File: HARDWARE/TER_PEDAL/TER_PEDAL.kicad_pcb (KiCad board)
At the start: 4 copper layers, 78.2 x 40 mm, 63 parts, among them J1 DEBUG, J2 APPS_1, J3 RJ45_Shielded, J4 APPS_2, J5 BPPS_1, SW1 RST, U1 STM32F103C8Tx, U2 AOZ1280CI, U3 LM1117MP-3.3, U4 SN65HVD230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

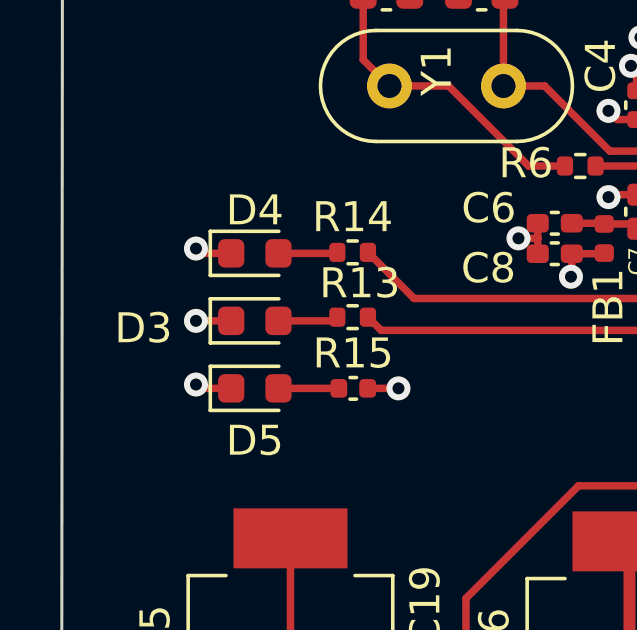
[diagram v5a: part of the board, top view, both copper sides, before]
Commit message: Changed Pinout and added status leds silkmask
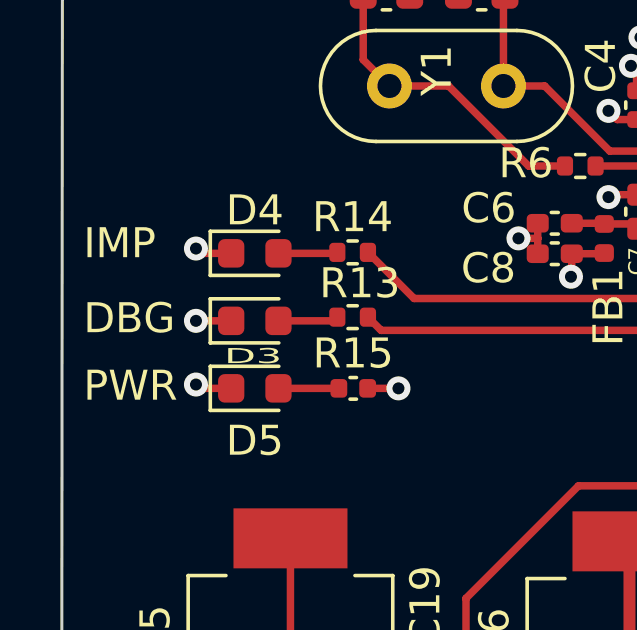
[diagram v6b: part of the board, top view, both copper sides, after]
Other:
- board text added: "DBG"
- board text added: "IMP"
- board text added: "PWR"
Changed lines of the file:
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@@
     (property "ki_keywords" "LED diode")
     (attr smd)
-    (fp_text reference "D3" (at -3.7125 0.25) (layer "F.SilkS")
-        (effects (font (size 1 1) (thickness 0.15)))
+    (fp_text reference "D3" (at -0.056699 1.175611) (layer "F.SilkS")
+        (effects (font (size 0.5 1) (thickness 0.125)))
     )
     (fp_text value "LED" (at 0 1.43) (layer "F.Fab")
@@
   (gr_line (start 114.3 75) (end 187.5 75)
     (stroke (width 0.1) (type default)) (layer "Edge.Cuts"))
+  (gr_text "PWR\n" (at 112.5 93.75) (layer "F.SilkS")
+    (effects (font (size 1 1) (thickness 0.15)) (justify left bottom))
+  )
+  (gr_text "IMP" (at 112.5 89) (layer "F.SilkS")
+    (effects (font (size 1 1) (thickness 0.15)) (justify left bottom))
+  )
+  (gr_text "DBG" (at 112.5 91.5) (layer "F.SilkS")
+    (effects (font (size 1 1) (thickness 0.15)) (justify left bottom))
+  )
   (segment (start 139.6715 91.3335) (end 139.43 91.092) (width 0.25) (layer "F.Cu") (net 1))
   (segment (start 140.8425 83.342) (end 141.93 83.342) (width 0.25) (layer "F.Cu") (net 1))

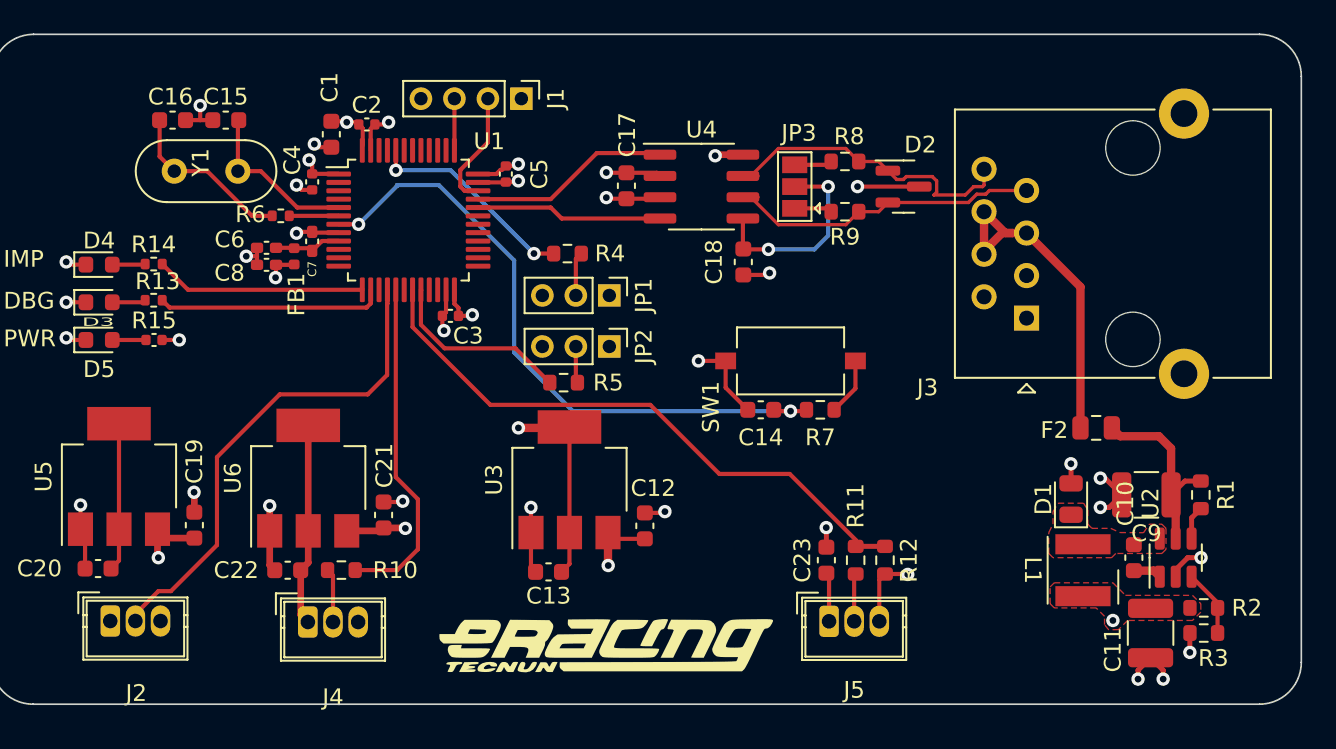
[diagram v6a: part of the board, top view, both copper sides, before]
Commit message: Swapped Custom Supply for traco for simplicity
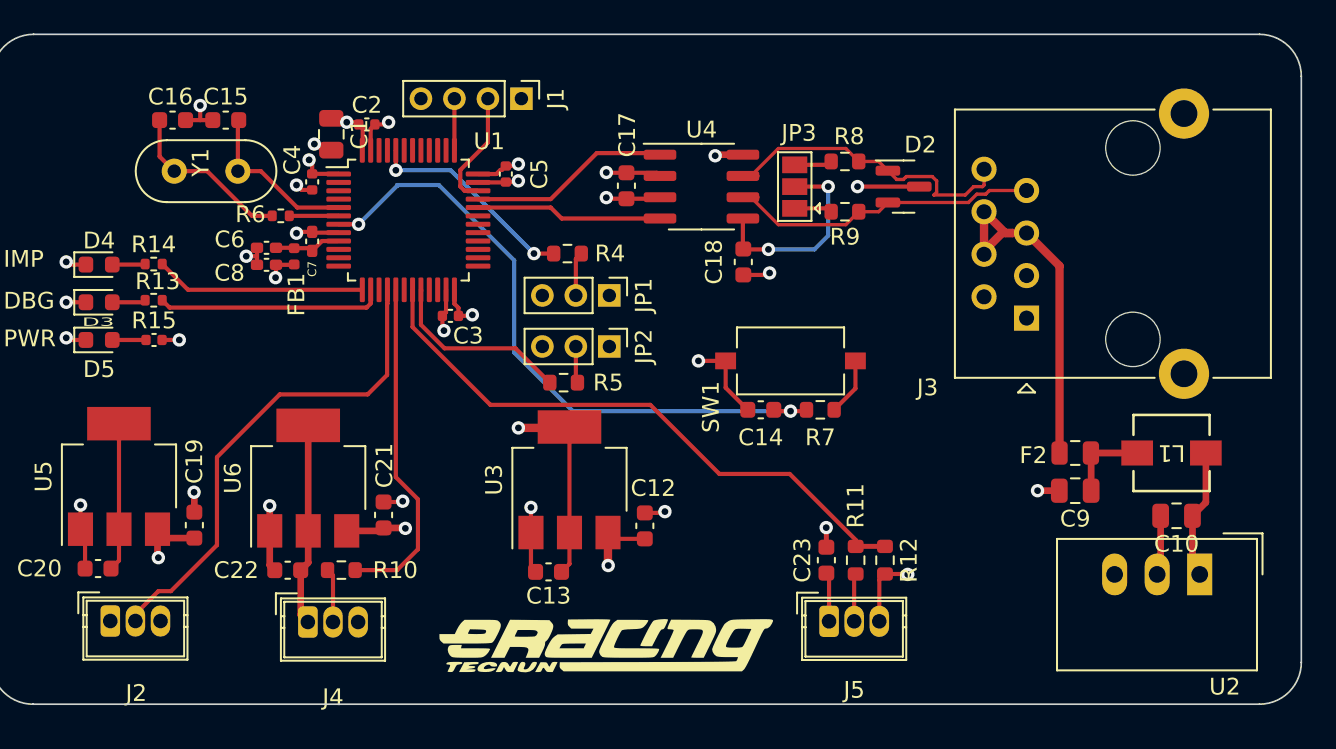
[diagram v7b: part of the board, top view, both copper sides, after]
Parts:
- removed C11: 10u, Capacitor_SMD:C_1210_3225Metric
- removed D1: 36V 1A, Diode_SMD:D_0805_2012Metric
- removed R1: 10k, Resistor_SMD:R_0603_1608Metric
- removed R2: 49.9k, Resistor_SMD:R_0603_1608Metric
- removed R3: 9.53k, Resistor_SMD:R_0603_1608Metric
- C1: footprint Capacitor_SMD:C_0603_1608Metric -> Capacitor_SMD:C_0805_2012Metric
- C10: value 10n -> 10 µF; footprint Capacitor_SMD:C_0603_1608Metric -> Capacitor_SMD:C_0805_2012Metric
- C9: value 4.7u -> 10 µF; footprint Capacitor_SMD:C_1210_3225Metric -> Capacitor_SMD:C_0805_2012Metric
- L1: value 2.2u -> TCK-141; footprint Inductor_SMD_Wurth:L_Wurth_WE-LQSH-4020 -> Footprints:IND_TCK-141_TRP
- U2: value AOZ1280CI -> TSR_1-2450; footprint Package_TO_SOT_SMD:SOT-23-6 -> Converter_DCDC:Converter_DCDC_TRACO_TSR-1_THT
- moved L1 8.77 mm to (182.2, 100.0), turned to 180 degrees
- moved C9 4.26 mm to (176.5, 102.2)
- moved C10 3.57 mm to (182.6, 103.8), turned to 180 degrees
- moved F2 1.95 mm to (176.5, 100.0)
- moved U2 1.75 mm to (183.9, 107.2), turned to 180 degrees
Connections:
- C10 pad 1: Net-(U2-BST) -> Net-(U2-Vin)
- C10 pad 2: /POWER/SWTCH -> GND
- C9 pad 1: Net-(U2-VIN) -> Net-(C9-Pad1)
- F2 pad 2: Net-(U2-VIN) -> Net-(C9-Pad1)
- L1 pad 1: /POWER/SWTCH -> Net-(U2-Vin)
- L1 pad 2: +5V -> Net-(C9-Pad1)
- U2 pad 1: Net-(U2-BST) -> Net-(U2-Vin)
- U2 pad 3: /POWER/FeedBack -> +5V
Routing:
- net Net-(U2-VIN): track 11.7 -> 0.00 mm
- net Net-(U2-Vin): track 0.00 -> 7.76 mm
- net GND: track 67.4 -> 61.3 mm, vias 31 -> 25
- net Net-(C9-Pad1): track 0.00 -> 5.02 mm
- net /POWER/FeedBack: track 4.00 -> 0.00 mm
- net Net-(U2-EN): track 2.02 -> 0.00 mm
- net Net-(U2-BST): track 1.70 -> 0.00 mm
- net +24V: track 20.8 -> 21.8 mm
- net +5V: vias 4 -> 3
- removed copper zone on F.Cu, net +5V
- removed copper zone on F.Cu, net /POWER/SWTCH

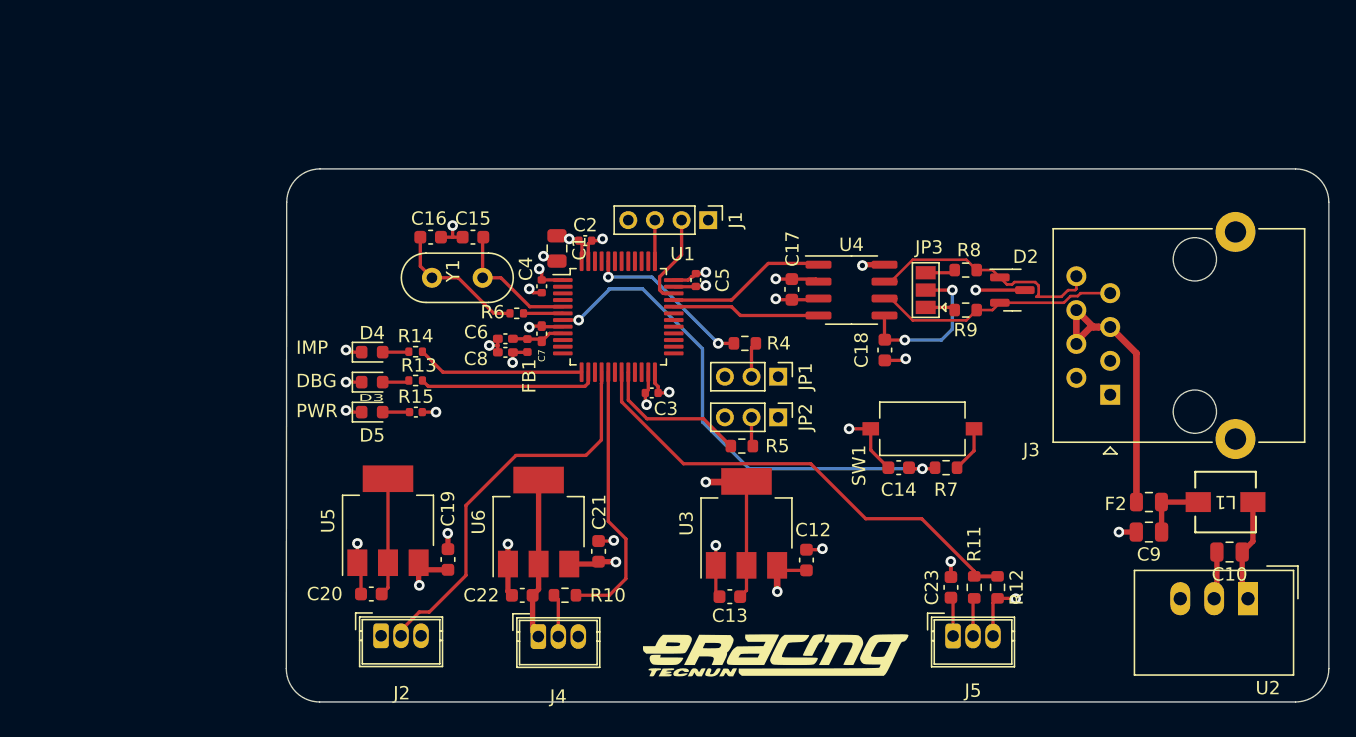
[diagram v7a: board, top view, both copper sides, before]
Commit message: The RJ45 pinout was incorrect according to the poe standard, started redesign and relocation of the board revision
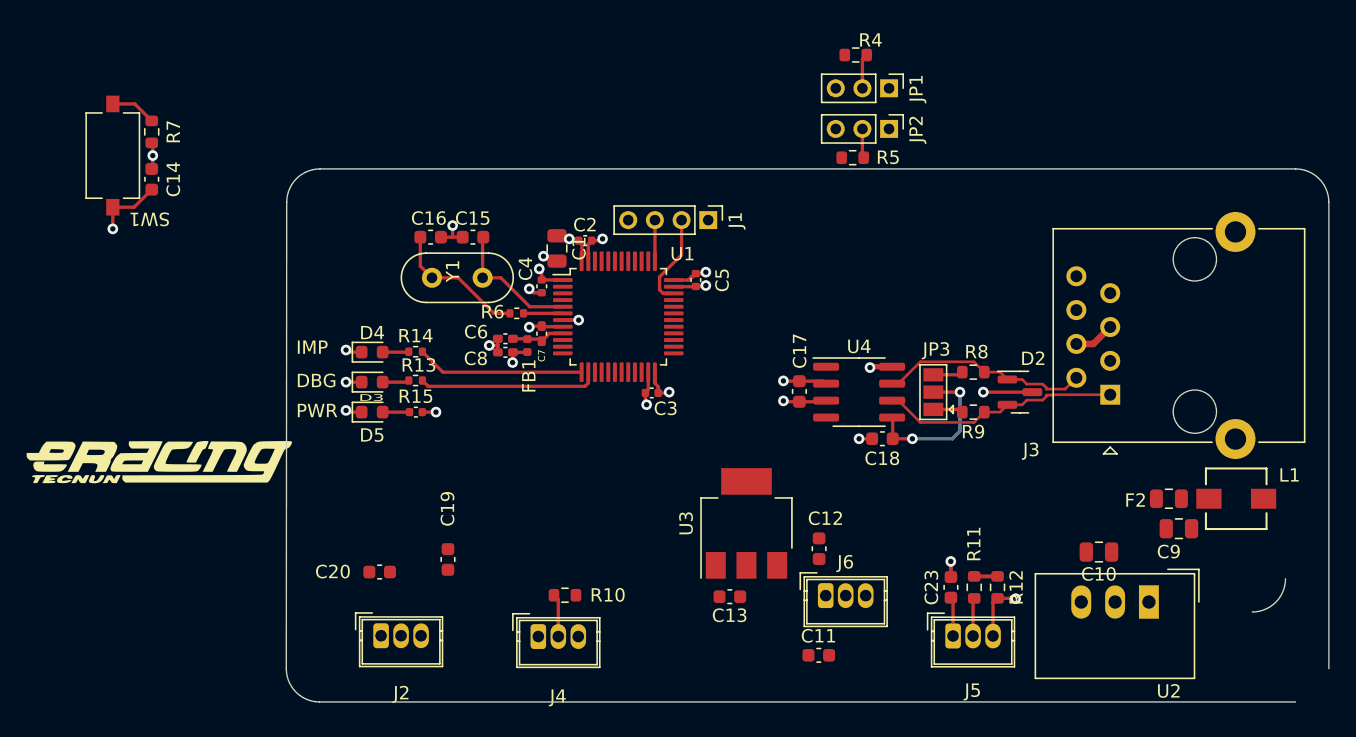
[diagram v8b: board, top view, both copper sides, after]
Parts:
- removed C21, C22: 10u, Capacitor_SMD:C_0603_1608Metric
- removed U5, U6: LM1117MP-3.3, Package_TO_SOT_SMD:SOT-223-3_TabPin2
- added C11: 10u, Capacitor_SMD:C_0603_1608Metric, F.Cu at (151.7, 111.5)
- added J6: SteerSensor, Connector_Wuerth:Wuerth_WR-WTB_64800311622_1x03_P1.50mm_Vertical, F.Cu at (152.2, 107.0)
- moved R7 64.7 mm to (101.7, 72.2), turned to -90 degrees
- moved SW1 64.1 mm to (98.8, 74.0), turned to 90 degrees
- moved C14 60.1 mm to (101.7, 75.8), turned to -90 degrees
- moved G*** 48.5 mm to (102.2, 97.0)
- moved R5 23.2 mm to (154.3, 74.2)
- moved JP1 23.2 mm to (157.0, 69.0)
- moved JP2 23.2 mm to (157.0, 72.0)
- moved R4 23.2 mm to (154.5, 66.5)
- moved C10 9.80 mm to (172.8, 103.8)
- moved C17 7.68 mm to (150.3, 91.7)
- moved D2 7.68 mm to (166.8, 91.8)
- moved JP3 7.68 mm to (160.3, 91.8)
- moved R8 7.68 mm to (163.3, 90.2)
- moved R9 7.68 mm to (163.3, 93.2)
- moved U4 7.68 mm to (154.8, 91.8)
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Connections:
- C19 pad 1: +5V -> /SENSORS/SENS_1
- C20 pad 1: /SENSORS/VCC_1 -> /MICRO/STEER_ADC
- J2 pad 1: /SENSORS/VCC_1 -> +3.3V
- J3 pad 1: GND -> /CAN/CAN-
- J3 pad 2: GND -> /CAN/CAN+
- J3 pad 3: GND -> unconnected-(J3-Pad3)
- J3 pad 6: +24V -> unconnected-(J3-Pad6)
- J3 pad 7: /CAN/CAN- -> GND
- J3 pad 8: /CAN/CAN+ -> GND
- J4 pad 1: /SENSORS/VCC_2 -> +3.3V
- U1 pad 18: unconnected-(U1-PB0-Pad18) -> /MICRO/STEER_ADC
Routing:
- net /MICRO/NRST: track 38.8 -> 3.21 mm
- net /MICRO/BPPS_ADC: track 36.1 -> 1.75 mm
- net /SENSORS/SENS_1: track 29.5 -> 0.00 mm
- net GND: track 61.3 -> 40.7 mm, vias 25 -> 18
- net /MICRO/APPS_2_ADC: track 20.3 -> 0.00 mm
- net +24V: track 21.8 -> 3.07 mm
- net /MICRO/BOOT0: track 12.7 -> 0.00 mm, vias 2 -> 0
- net /SENSORS/VCC_2: track 12.1 -> 0.00 mm
- net /CAN/CAN_TX: track 12.0 -> 0.00 mm
- net +3.3V: track 28.8 -> 16.9 mm, vias 8 -> 7
- net +5V: track 15.0 -> 3.47 mm, vias 3 -> 0
- net /MICRO/BOOT1: track 11.2 -> 0.04 mm
- net /CAN/CAN_RX: track 11.1 -> 0.00 mm
- net /SENSORS/VCC_1: track 8.85 -> 0.00 mm
- net Net-(U2-Vin): track 7.76 -> 0.00 mm
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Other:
- outline, holes or cut-outs redrawn
